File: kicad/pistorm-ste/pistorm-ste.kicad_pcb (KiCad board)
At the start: 4 copper layers, 118 x 70.5 mm, 27 parts, among them J1 Raspberry_Pi_2_3, U1 SN54CBTD3384, U2 SN74LVC16373, U3 SN74LVC16373, U4 EPM240T100, U5 SN74LVC16373, U6 SN74LVC16373, U7 SN54CBTD3384, U8 LM1117-3.3

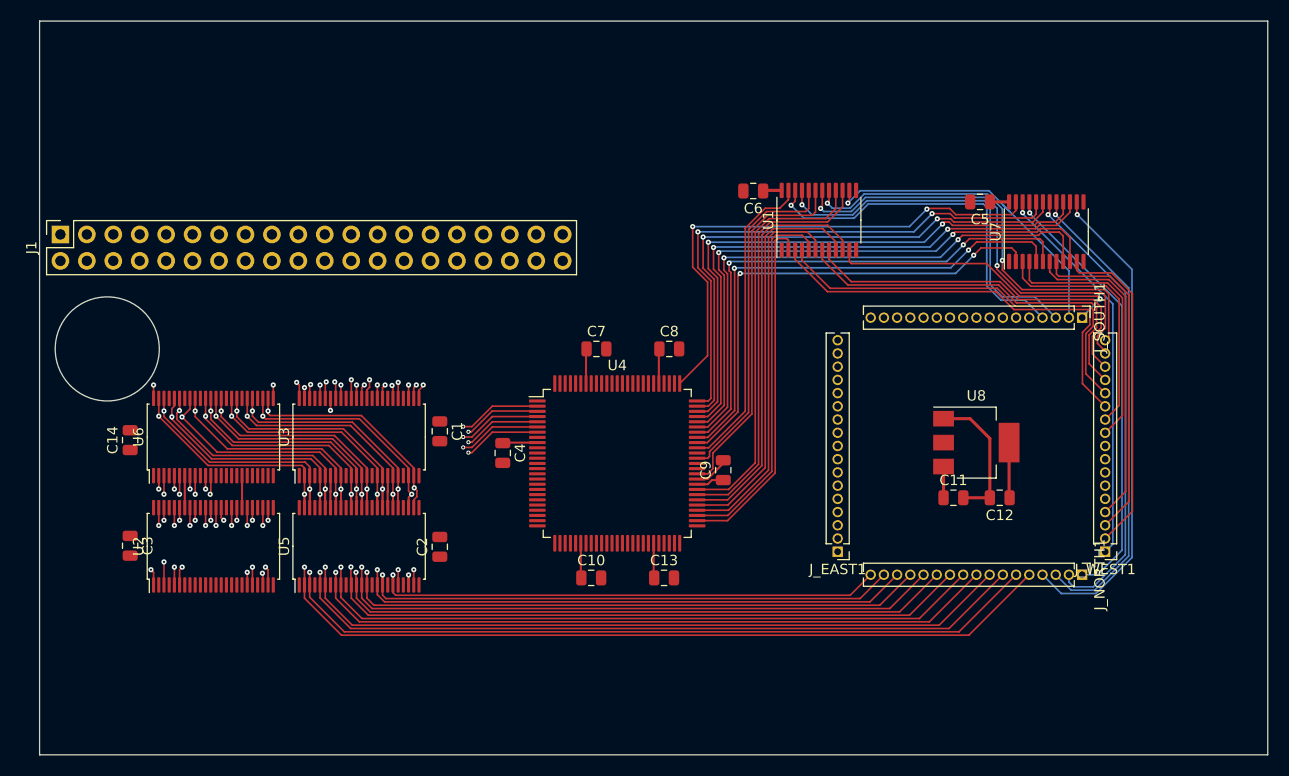
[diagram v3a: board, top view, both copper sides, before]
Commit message: squishing up to avoid post
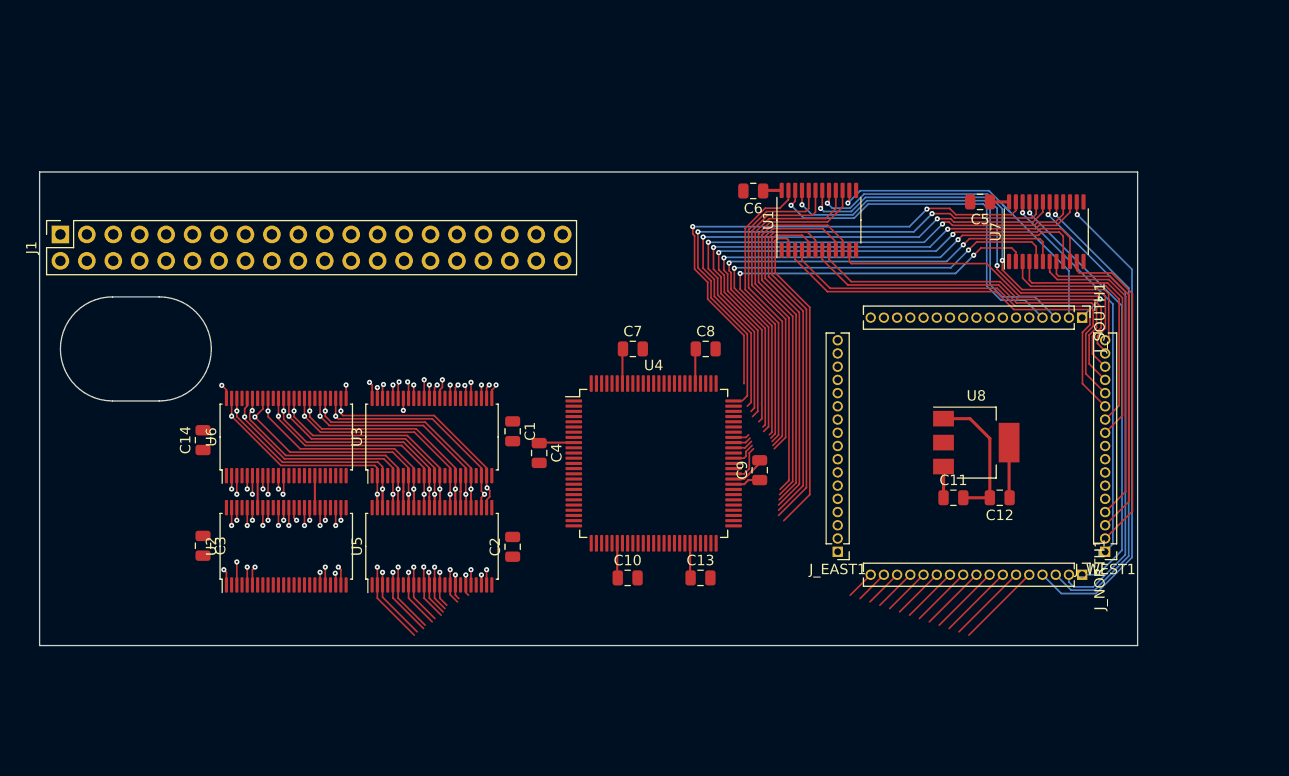
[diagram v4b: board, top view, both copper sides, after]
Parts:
- moved C1 7.00 mm to (104.6, 138.4)
- moved C14 7.00 mm to (74.8, 139.2)
- moved C2 7.00 mm to (104.6, 149.5)
- moved C3 7.00 mm to (74.8, 149.4)
- moved U2 7.00 mm to (82.8, 149.4)
- moved U3 7.00 mm to (96.8, 138.9)
- moved U5 7.00 mm to (96.8, 149.4)
- moved U6 7.00 mm to (82.8, 138.9)
- moved C10 3.50 mm to (115.6, 152.4)
- moved C13 3.50 mm to (122.6, 152.4)
- moved C4 3.50 mm to (107.1, 140.4)
- moved C7 3.50 mm to (116.1, 130.4)
- moved C8 3.50 mm to (123.1, 130.4)
- moved C9 3.50 mm to (128.3, 142.1)
- moved U4 3.50 mm to (118.1, 141.4)
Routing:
- net /D0: track 96.3 -> 36.0 mm
- net /D1: track 95.0 -> 35.9 mm
- net /D2: track 92.9 -> 35.4 mm
- net /D3: track 91.7 -> 35.3 mm
- net /D4: track 89.6 -> 34.9 mm
- net /D5: track 86.1 -> 32.6 mm
- net /D6: track 84.2 -> 32.2 mm
- net /D7: track 80.4 -> 29.5 mm
- net /D8: track 78.3 -> 28.6 mm
- net /D9: track 78.1 -> 29.5 mm
- net /D10: track 74.8 -> 28.2 mm
- net /D11: track 72.6 -> 27.1 mm
- net /D12: track 70.4 -> 26.7 mm
- net /SD4: track 62.1 -> 54.2 mm, vias 4 -> 3
- net /SD2: track 62.2 -> 54.3 mm, vias 4 -> 3
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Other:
- board size 118 x 70.5 mm -> 105.5 x 45.5 mm

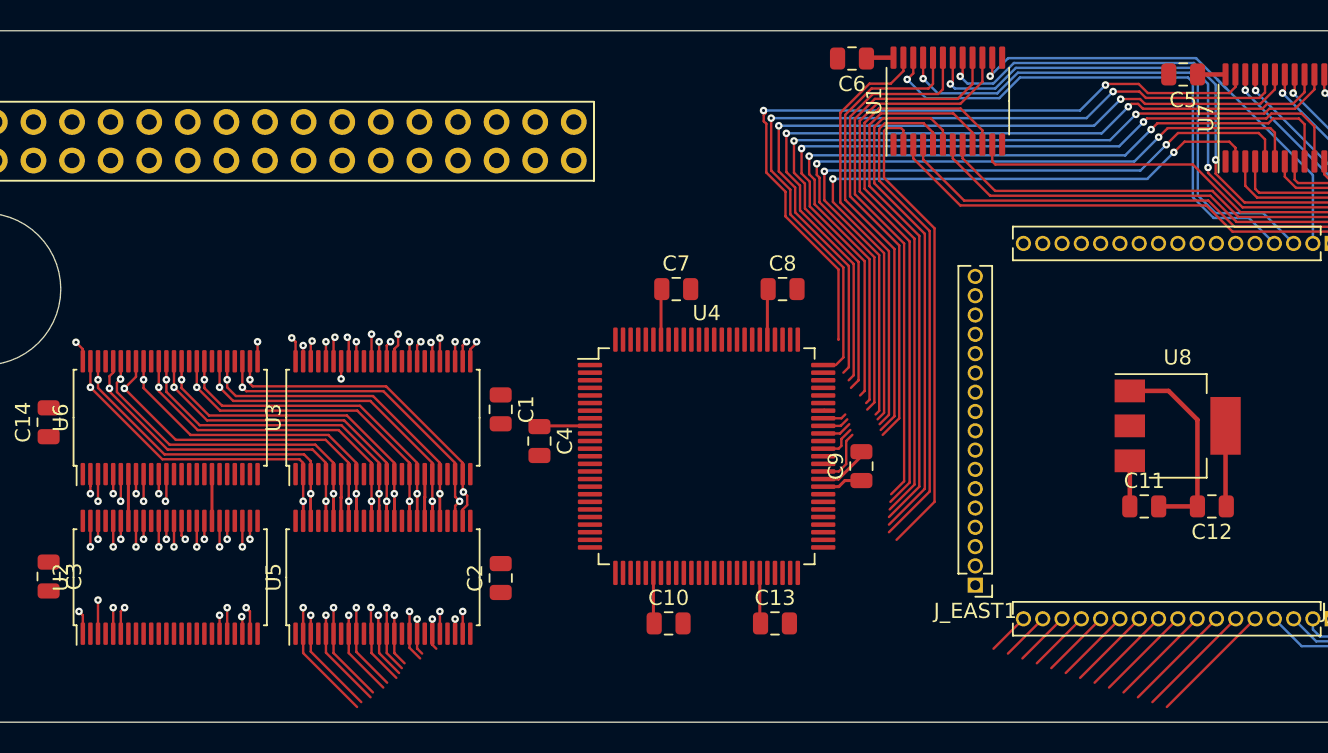
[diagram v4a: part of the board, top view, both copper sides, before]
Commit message: Started routeing address lines
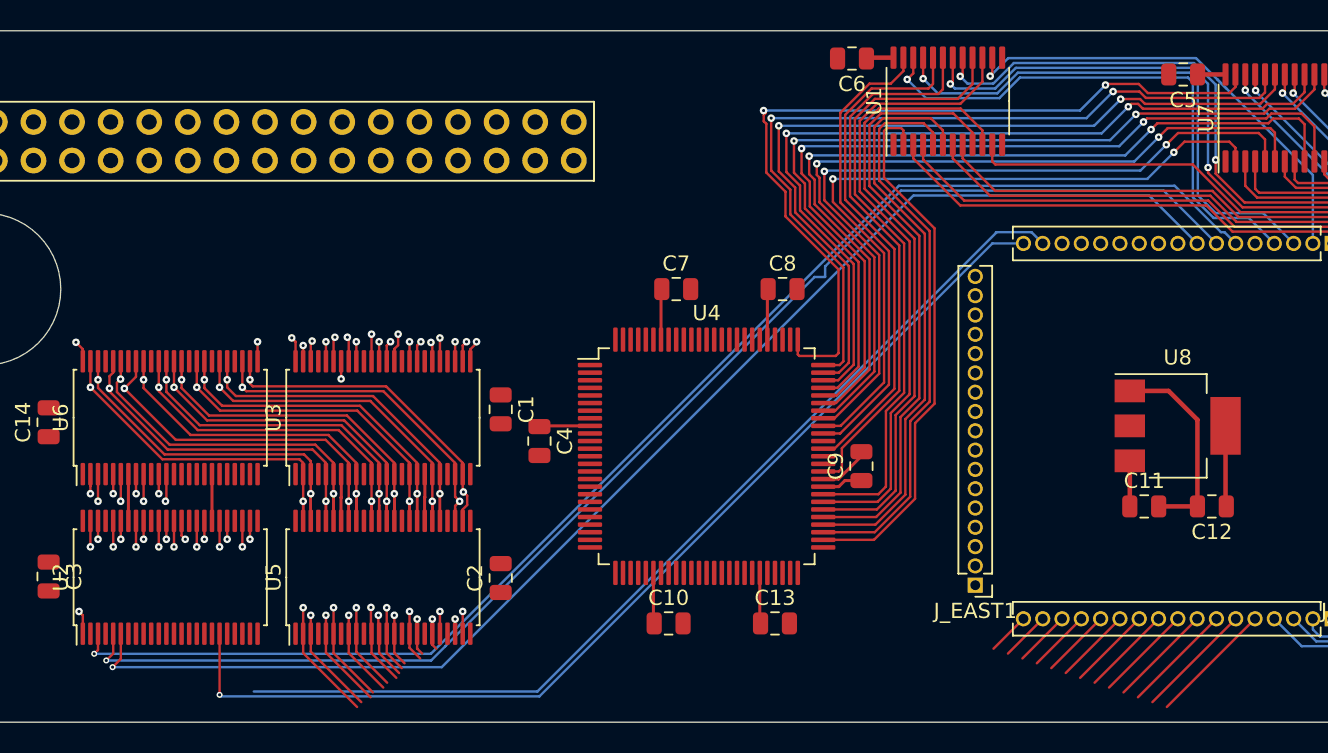
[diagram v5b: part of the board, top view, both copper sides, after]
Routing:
- net /A1: track 2.21 -> 90.9 mm
- net /A2: track 1.71 -> 89.7 mm
- net /A3: track 1.82 -> 88.0 mm
- net /A12: track 1.21 -> 69.3 mm
- net /A11: track 0.00 -> 64.8 mm
- net /DTACK_3: track 50.3 -> 54.9 mm
- net /IPL1_3: track 36.8 -> 40.8 mm
- net /VMA_3: track 31.7 -> 35.6 mm
- net /FC2_3: track 37.7 -> 41.6 mm
- net /IPL0_3: track 37.2 -> 41.0 mm
- net /BERR_3: track 36.4 -> 40.2 mm
- net /VPA_3: track 34.5 -> 38.4 mm
- net /E_3: track 33.8 -> 37.6 mm
- net /A15: track 1.82 -> 0.00 mm, vias 1 -> 0
- net /BR_3: track 51.2 -> 52.9 mm
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
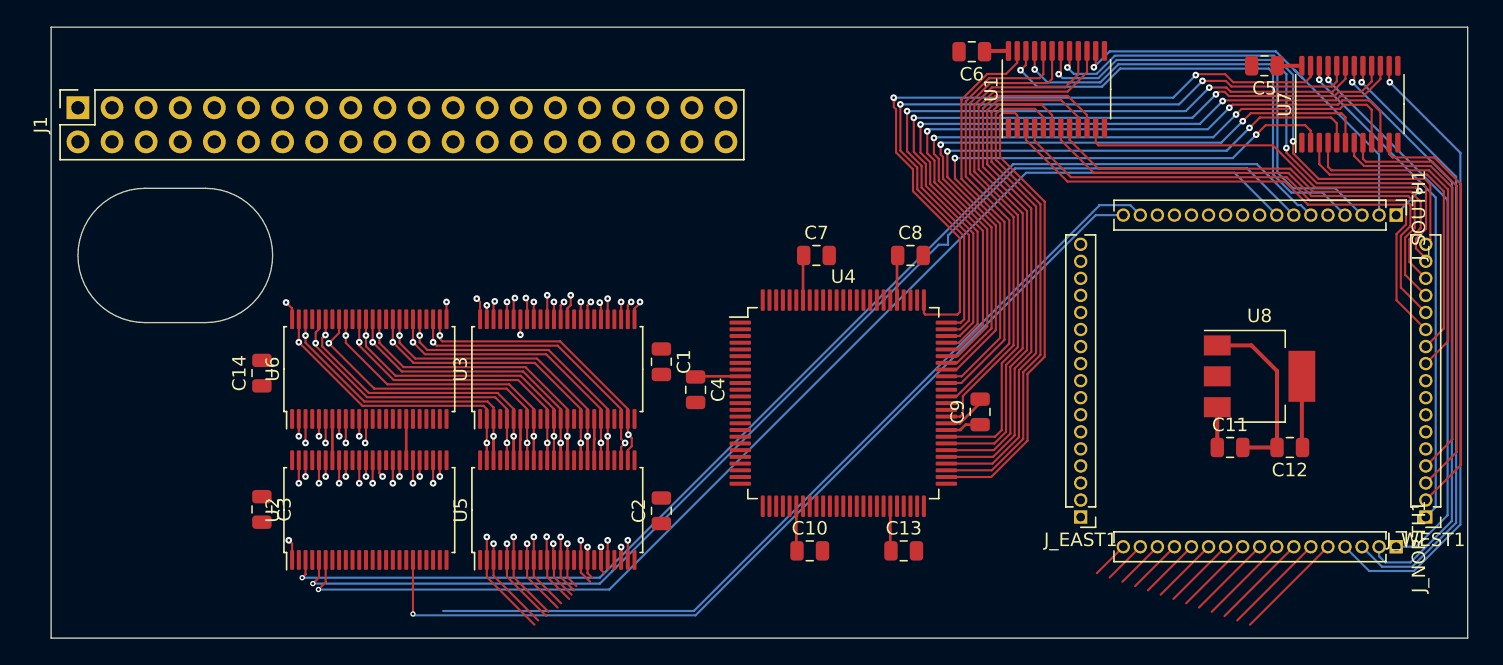
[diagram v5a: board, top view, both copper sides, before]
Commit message: Most major connections done. South-side CPLD to work on next
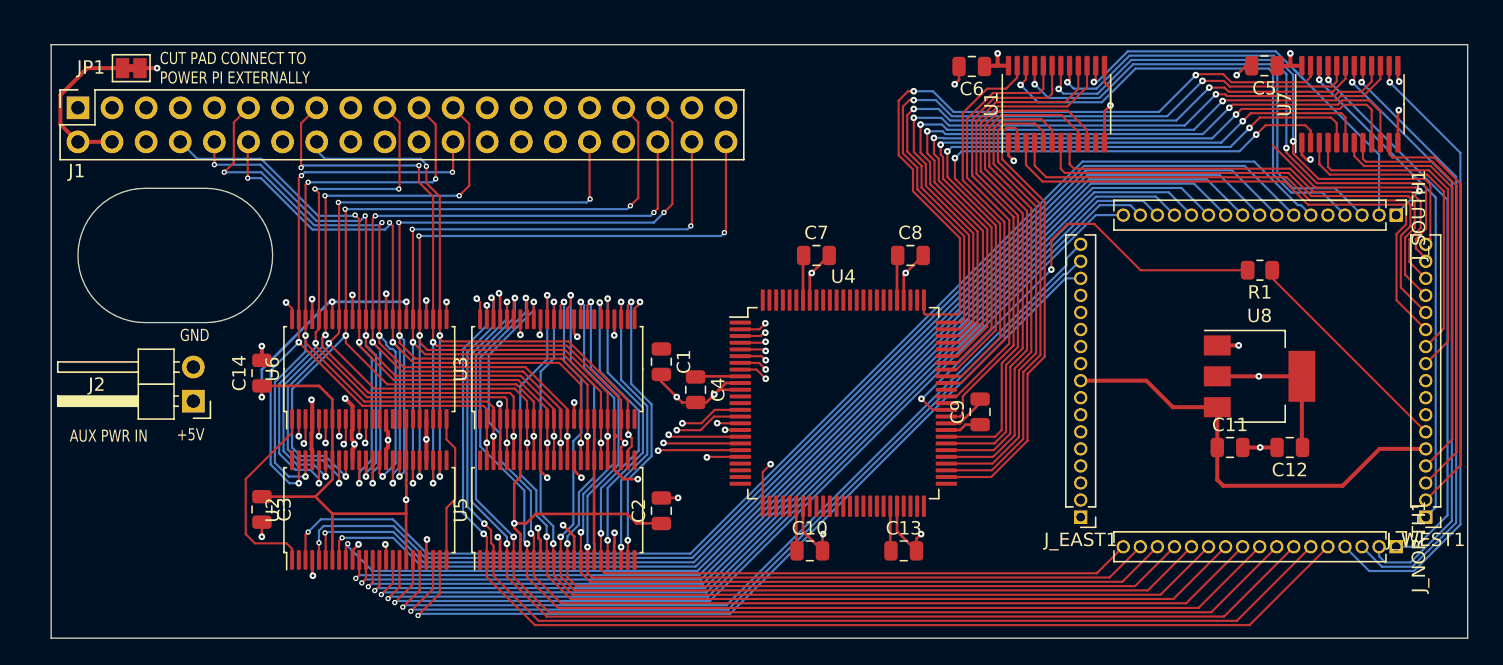
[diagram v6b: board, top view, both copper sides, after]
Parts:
- added J2: Conn_01x02_Male, Connector_PinHeader_2.54mm:PinHeader_1x02_P2.54mm_Horizontal, F.Cu at (69.7, 141.3)
- added JP1: SolderJumper_2_Bridged, Jumper:SolderJumper-2_P1.3mm_Bridged_Pad1.0x1.5mm, F.Cu at (65.1, 116.5)
- added R1: 0-100R, Resistor_SMD:R_0805_2012Metric, F.Cu at (149.1, 131.6)
- moved C6 1.10 mm to (127.7, 116.4)
- moved U1 1.10 mm to (134.0, 119.2)
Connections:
- J1 pad 2: +5V -> /+5V_PI
- J1 pad 4: +5V -> /+5V_PI
- J_WEST1 pad 6: /CLK -> /CLK_STE
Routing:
- net +5V: track 6.64 -> 201.3 mm, vias 0 -> 3
- net +3V3: track 38.2 -> 155.3 mm, vias 1 -> 7
- net GND: track 16.6 -> 114.4 mm, vias 0 -> 44
- net /A4: track 0.00 -> 84.3 mm, vias 0 -> 1
- net /A5: track 0.00 -> 82.0 mm, vias 0 -> 1
- net /A6: track 0.00 -> 79.4 mm, vias 0 -> 1
- net /A7: track 0.00 -> 77.9 mm, vias 0 -> 1
- net /A8: track 0.00 -> 76.3 mm, vias 0 -> 1
- net /A9: track 0.00 -> 74.7 mm, vias 0 -> 1
- net /A10: track 0.00 -> 73.3 mm, vias 0 -> 1
- net /A16: track 1.29 -> 73.7 mm
- net /A17: track 1.79 -> 73.7 mm
- net /A18: track 1.29 -> 71.1 mm
- net /A19: track 1.79 -> 70.9 mm
- net /A20: track 1.29 -> 68.6 mm
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- added copper zone on In1.Cu, net GND
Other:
- board size 105.5 x 45.5 mm -> 105.5 x 44.2 mm
- board text added: "+5V"
- board text added: "AUX PWR IN"
- board text added: "CUT PAD CONNECT TO POWER PI EXTERNALLY"
- board text added: "GND"

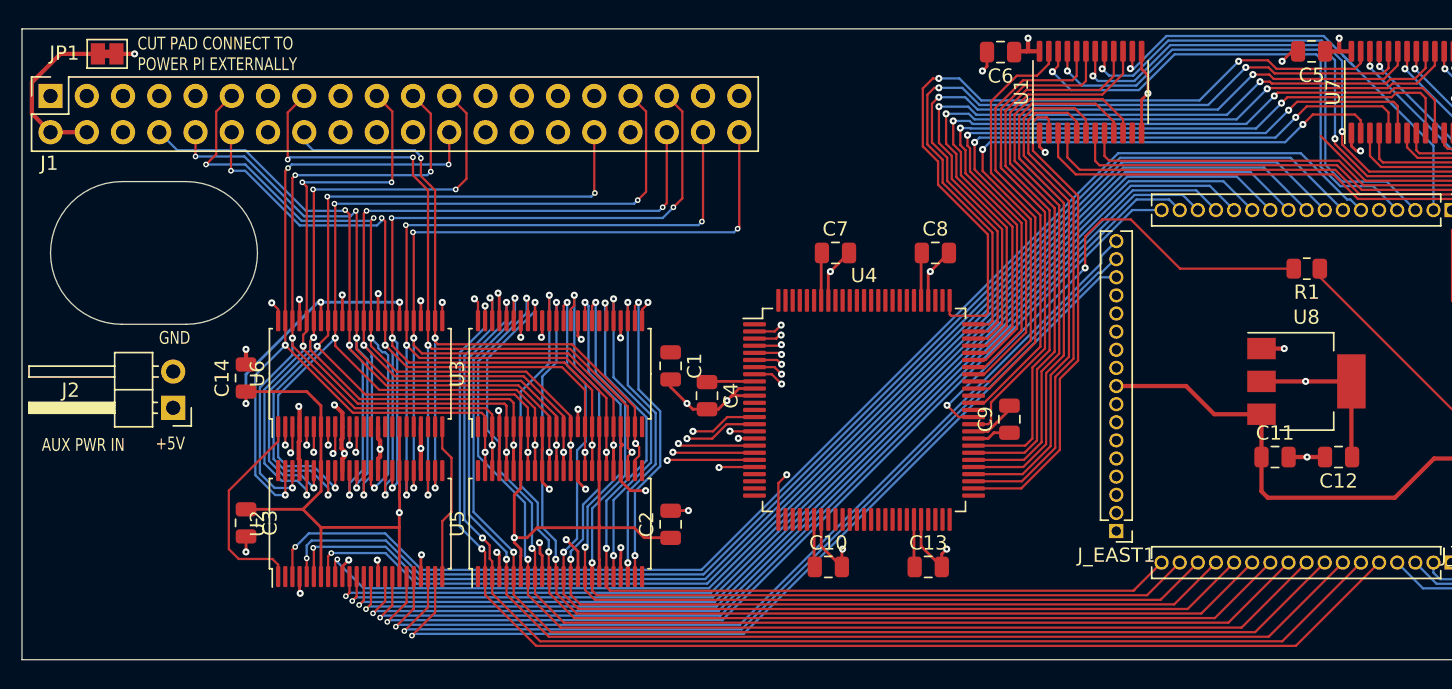
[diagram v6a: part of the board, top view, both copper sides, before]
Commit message: Primary routeing completed. Many DRC errors.
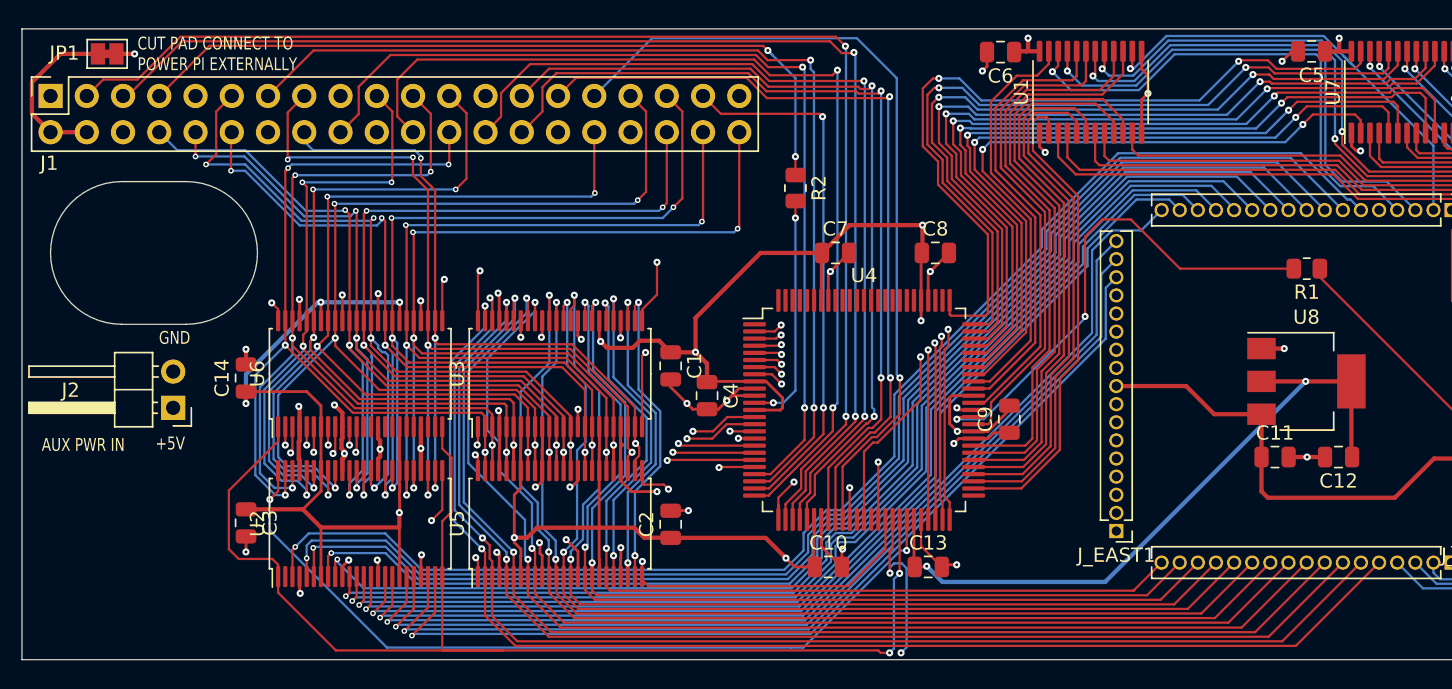
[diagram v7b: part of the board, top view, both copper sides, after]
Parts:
- added R2: 0-100R, Resistor_SMD:R_0805_2012Metric, F.Cu at (113.3, 125.9)
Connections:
- J1 pad 7: /PICLK -> /PICLK_OUT
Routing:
- net +3V3: track 155.3 -> 296.9 mm, vias 7 -> 15
- net /SA2: track 0.00 -> 90.1 mm, vias 0 -> 2
- net /SA1: track 0.00 -> 87.8 mm, vias 0 -> 2
- net /TDI: track 0.00 -> 71.6 mm, vias 0 -> 2
- net /TDO: track 0.00 -> 69.0 mm, vias 0 -> 2
- net /TMS: track 0.00 -> 66.8 mm, vias 0 -> 2
- net /ADDR_OE: track 25.8 -> 90.5 mm, vias 0 -> 2
- net /SWE: track 0.00 -> 62.6 mm, vias 0 -> 2
- net /ADDR_LTCH_16: track 1.44 -> 62.1 mm, vias 1 -> 2
- net /AUX1: track 0.00 -> 60.3 mm, vias 0 -> 2
- net /AUX0: track 0.00 -> 58.5 mm, vias 0 -> 2
- net /DATA_RD_OE: track 0.00 -> 57.7 mm, vias 0 -> 3
- net /ADDR_LTCH_0: track 0.00 -> 57.5 mm, vias 0 -> 2
- net /SOE: track 0.00 -> 56.9 mm, vias 0 -> 1
- net /SA0: track 0.00 -> 55.9 mm, vias 0 -> 2
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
